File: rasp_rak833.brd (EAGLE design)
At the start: 65 x 56 mm, 22 parts, among them IC1 SHTC3, IC2 AMS1117-3.3, K1 PIN20X2

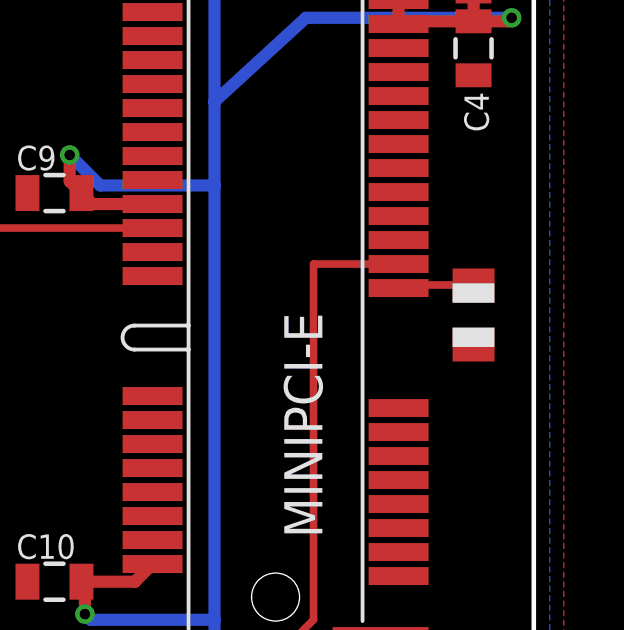
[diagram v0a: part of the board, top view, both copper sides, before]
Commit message: Board tested. Minor resistor value tweaks
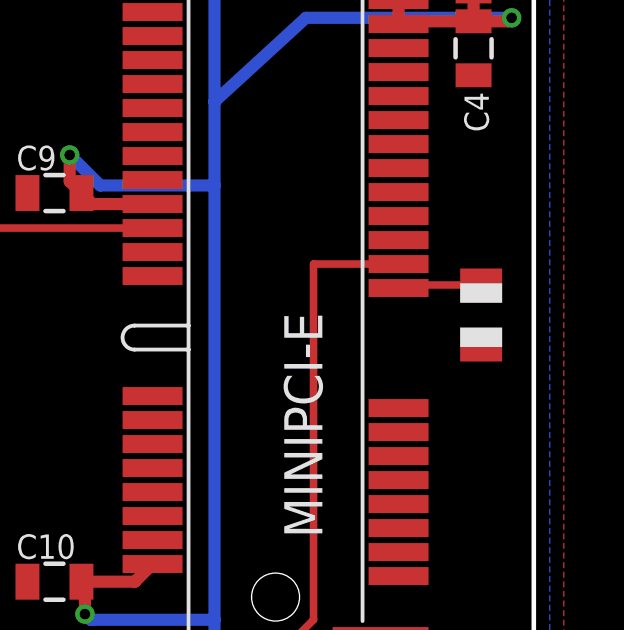
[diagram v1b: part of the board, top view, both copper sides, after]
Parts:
- R1: value 1K -> 50
- moved R2 0.25 mm to (63.2, 29.7)
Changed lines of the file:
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@@
 </element>
 <element name="PPS" library="adafruit" library_urn="urn:adsk.eagle:library:420" package="CHIP-LED0805" value="" x="40.132" y="13.97" rot="R180"/>
-<element name="R1" library="adafruit" library_urn="urn:adsk.eagle:library:420" package="R0805" value="1K" x="37.338" y="14.986" smashed="yes">
+<element name="R1" library="adafruit" library_urn="urn:adsk.eagle:library:420" package="R0805" value="50" x="37.338" y="14.986" smashed="yes">
 <attribute name="VALUE" x="36.576" y="12.7" size="1.27" layer="27"/>
 </element>
@@
 <element name="C9" library="xose" package="0805" value="0.1uF" x="49.022" y="33.782"/>
 <element name="C10" library="xose" package="0805" value="0.1uF" x="49.022" y="20.828"/>
-<element name="R2" library="adafruit" library_urn="urn:adsk.eagle:library:420" package="R0805" value="1K" x="62.992" y="29.718" smashed="yes" rot="R90">
-<attribute name="VALUE" x="65.278" y="28.956" size="1.27" layer="27" rot="R90"/>
+<element name="R2" library="adafruit" library_urn="urn:adsk.eagle:library:420" package="R0805" value="1K" x="63.246" y="29.718" smashed="yes" rot="R90">
+<attribute name="VALUE" x="65.532" y="28.956" size="1.27" layer="27" rot="R90"/>
 </element>
 <element name="C11" library="xose" package="0805" value="0.1uF" x="4.318" y="11.938" rot="R90"/>
@@
 <contactref element="R2" pad="2"/>
 <wire x1="60.492" y1="30.616" x2="60.594" y2="30.718" width="0.254" layer="1"/>
-<wire x1="60.594" y1="30.718" x2="62.992" y2="30.718" width="0.254" layer="1"/>
+<wire x1="60.594" y1="30.718" x2="63.246" y2="30.718" width="0.254" layer="1"/>
 </signal>
 <signal name="GPS_PPS">
